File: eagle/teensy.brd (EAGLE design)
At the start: 63.5 x 49.2 mm, 3 parts, among them SW2 282834-2

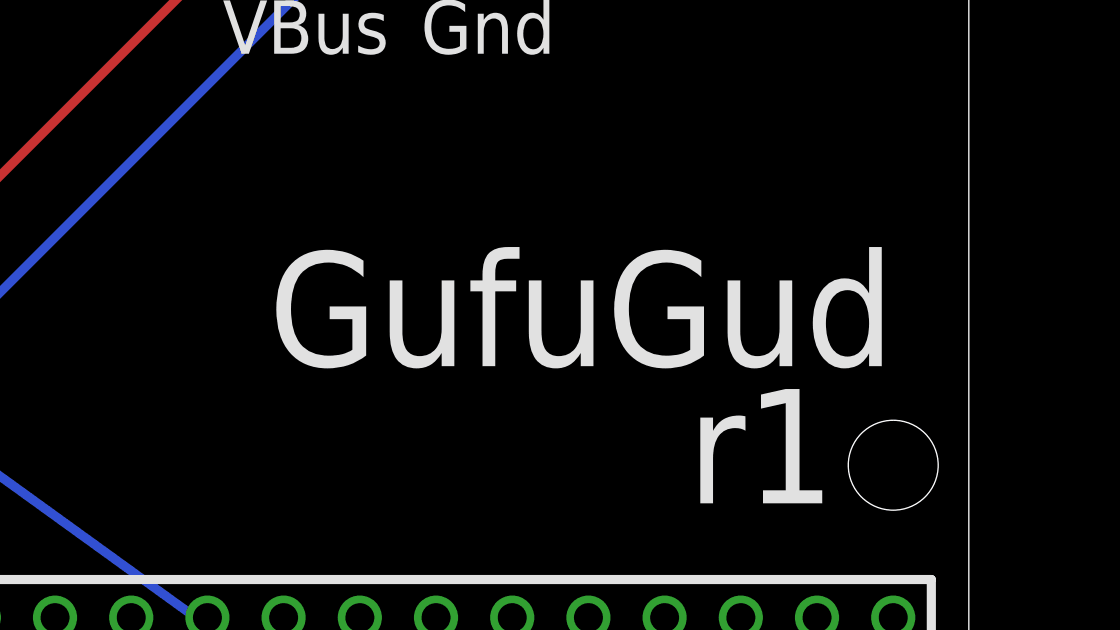
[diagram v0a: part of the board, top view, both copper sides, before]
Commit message: update and sync all schematics and images - fix labels and add consistent attribution
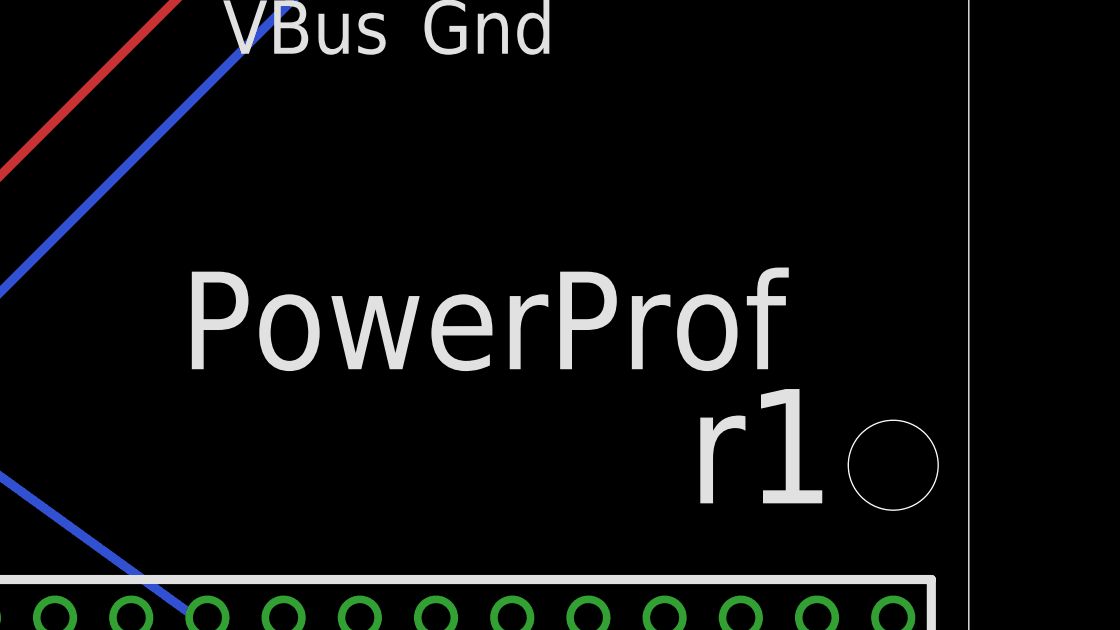
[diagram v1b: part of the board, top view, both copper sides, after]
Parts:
- SW2: value 282834-2 -> (none)
- renumbered U$1 to U1
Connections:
- net N$1 renamed VCC
- net N$2 renamed GND
- net N$3 renamed SCL
- net N$4 renamed SDA
- net N$5 renamed ALERT
- net N$8 renamed VBUS
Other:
- board text added: "MIT License - by ayan4m1"
- board text added: "PowerProf"
- board text added: "https://github.com/powerprof"
- board text removed: "GufuGud"
- board text removed: "by ayan4m1 and weeding_nerdy"

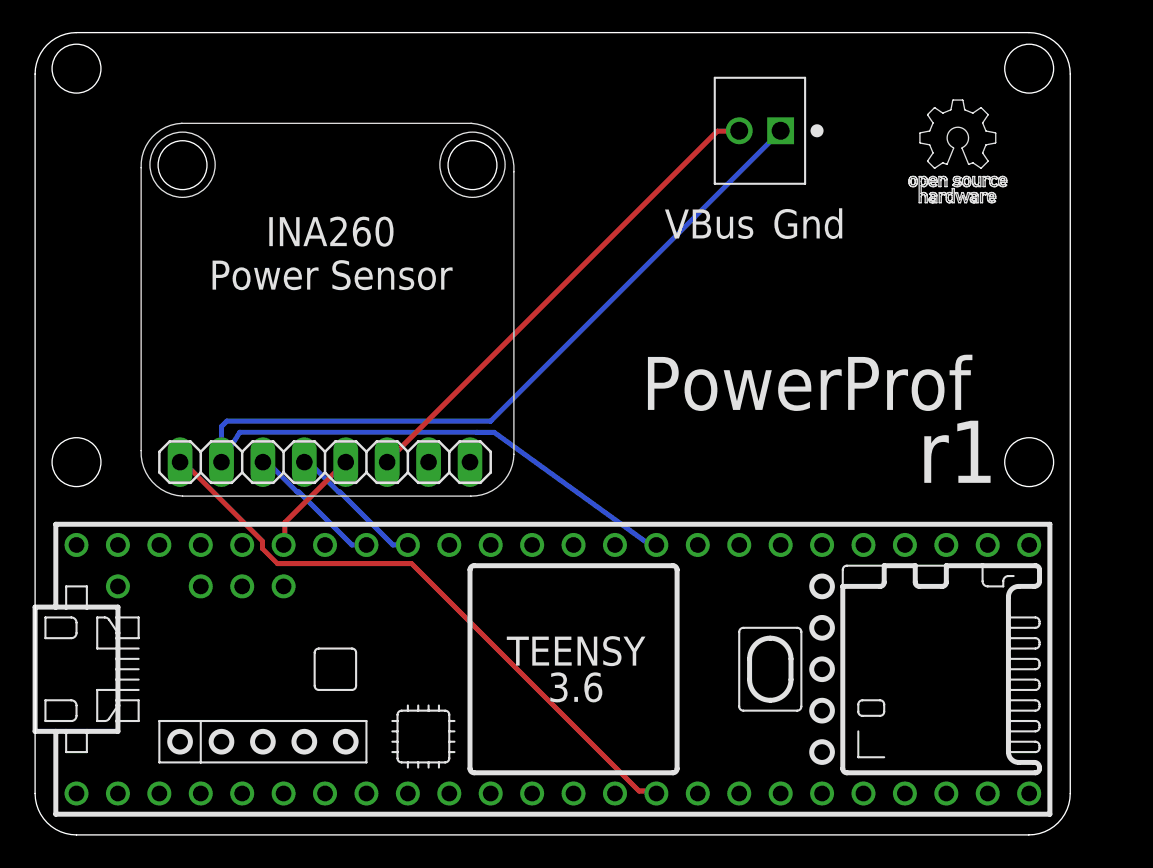
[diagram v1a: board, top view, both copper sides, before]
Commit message: update clearances to 8mil (thanks tech-tx!)
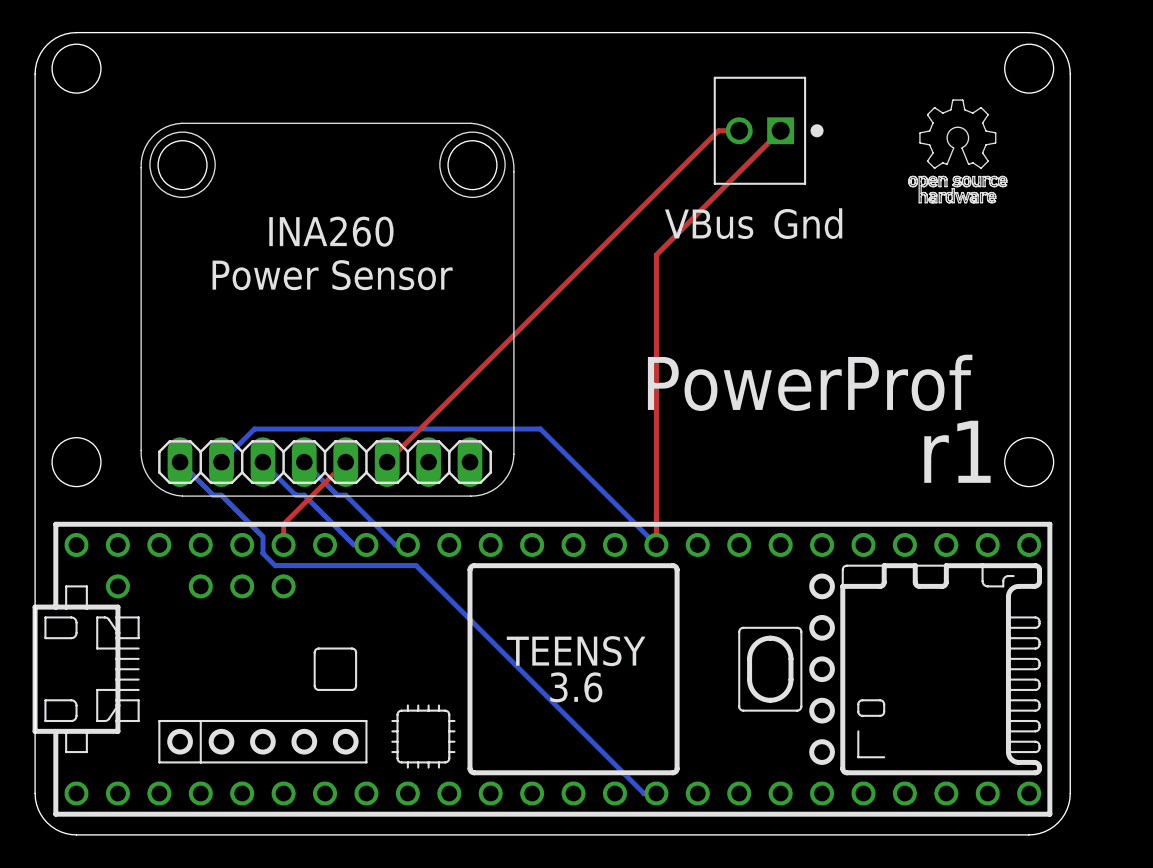
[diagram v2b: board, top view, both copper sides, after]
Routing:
- net GND: track 74.0 -> 59.0 mm
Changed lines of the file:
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@@
 <param name="mtCopper" value="0.035mm 0.035mm 0.035mm 0.035mm 0.035mm 0.035mm 0.035mm 0.035mm 0.035mm 0.035mm 0.035mm 0.035mm 0.035mm 0.035mm 0.035mm 0.035mm"/>
 <param name="mtIsolate" value="1.5mm 0.15mm 0.2mm 0.15mm 0.2mm 0.15mm 0.2mm 0.15mm 0.2mm 0.15mm 0.2mm 0.15mm 0.2mm 0.15mm 0.2mm"/>
-<param name="mdWireWire" value="6mil"/>
-<param name="mdWirePad" value="6mil"/>
-<param name="mdWireVia" value="6mil"/>
-<param name="mdPadPad" value="6mil"/>
-<param name="mdPadVia" value="6mil"/>
-<param name="mdViaVia" value="6mil"/>
-<param name="mdSmdPad" value="6mil"/>
-<param name="mdSmdVia" value="6mil"/>
-<param name="mdSmdSmd" value="6mil"/>
+<param name="mdWireWire" value="8mil"/>
+<param name="mdWirePad" value="8mil"/>
+<param name="mdWireVia" value="8mil"/>
+<param name="mdPadPad" value="8mil"/>
+<param name="mdPadVia" value="8mil"/>
+<param name="mdViaVia" value="8mil"/>
+<param name="mdSmdPad" value="8mil"/>
+<param name="mdSmdVia" value="8mil"/>
+<param name="mdSmdSmd" value="8mil"/>
 <param name="mdViaViaSameLayer" value="6mil"/>
 <param name="mnLayersViaInSmd" value="2"/>
@@
 <signal name="VCC">
 <contactref element="U1" pad="3V3"/>
-<wire x1="37.0332" y1="53.4924" x2="37.9476" y2="53.4924" width="0.3048" layer="1"/>
-<wire x1="23.0886" y1="67.437" x2="37.0332" y2="53.4924" width="0.3048" layer="1"/>
-<wire x1="14.859" y1="67.437" x2="23.0886" y2="67.437" width="0.3048" layer="1"/>
-<wire x1="13.9446" y1="68.3514" x2="14.859" y2="67.437" width="0.3048" layer="1"/>
-<wire x1="13.9446" y1="68.8086" x2="13.9446" y2="68.3514" width="0.3048" layer="1"/>
-<wire x1="8.9154" y1="73.8378" x2="13.9446" y2="68.8086" width="0.3048" layer="1"/>
-<wire x1="37.9476" y1="53.4924" x2="38.1" y2="53.34" width="0.3048" layer="1"/>
 <contactref element="JP1" pad="1"/>
-<wire x1="8.9154" y1="73.8378" x2="8.89" y2="73.66" width="0.3048" layer="1"/>
+<wire x1="37.338" y1="53.34" x2="38.1" y2="53.34" width="0.3048" layer="16"/>
+<wire x1="23.368" y1="67.31" x2="37.338" y2="53.34" width="0.3048" layer="16"/>
+<wire x1="14.732" y1="67.31" x2="23.368" y2="67.31" width="0.3048" layer="16"/>
+<wire x1="13.97" y1="68.072" x2="14.732" y2="67.31" width="0.3048" layer="16"/>
+<wire x1="13.97" y1="69.088" x2="13.97" y2="68.072" width="0.3048" layer="16"/>
+<wire x1="11.43" y1="71.628" x2="13.97" y2="69.088" width="0.3048" layer="16"/>
+<wire x1="10.922" y1="71.628" x2="11.43" y2="71.628" width="0.3048" layer="16"/>
+<wire x1="8.89" y1="73.66" x2="10.922" y2="71.628" width="0.3048" layer="16"/>
 </signal>
 <signal name="GND">
 <contactref element="SW2" pad="1"/>
 <contactref element="U1" pad="GND2"/>
-<wire x1="38.1762" y1="68.58" x2="38.1" y2="68.58" width="0.3048" layer="16"/>
-<wire x1="45.72" y1="93.98" x2="45.72" y2="93.9546" width="0.3048" layer="16"/>
-<wire x1="45.72" y1="93.9546" x2="27.94" y2="76.1746" width="0.3048" layer="16"/>
-<wire x1="27.94" y1="76.1746" x2="11.7602" y2="76.1746" width="0.3048" layer="16"/>
-<wire x1="11.43" y1="75.8444" x2="11.43" y2="73.66" width="0.3048" layer="16"/>
 <contactref element="JP1" pad="2"/>
-<wire x1="37.713109375" y1="68.58" x2="38.1" y2="68.58" width="0.3048" layer="16"/>
-<wire x1="37.713109375" y1="68.58" x2="28.153121875" y2="75.487215625" width="0.3048" layer="16"/>
-<wire x1="28.153121875" y1="75.487215625" x2="27.113471875" y2="75.487215625" width="0.3048" layer="16"/>
-<wire x1="27.113471875" y1="75.487215625" x2="27.1118875" y2="75.4888" width="0.3048" layer="16"/>
-<wire x1="12.5476" y1="75.4888" x2="11.43" y2="73.66" width="0.3048" layer="16"/>
-<wire x1="27.1118875" y1="75.4888" x2="12.5476" y2="75.4888" width="0.3048" layer="16"/>
-<wire x1="11.7602" y1="76.1746" x2="11.43" y2="75.8444" width="0.3048" layer="16"/>
+<wire x1="38.1" y1="86.36" x2="38.1" y2="68.58" width="0.3048" layer="1"/>
+<wire x1="45.72" y1="93.98" x2="38.1" y2="86.36" width="0.3048" layer="1"/>
+<wire x1="13.462" y1="75.692" x2="11.43" y2="73.66" width="0.3048" layer="16"/>
+<wire x1="30.988" y1="75.692" x2="13.462" y2="75.692" width="0.3048" layer="16"/>
+<wire x1="38.1" y1="68.58" x2="30.988" y2="75.692" width="0.3048" layer="16"/>
 </signal>
 <signal name="SCL">
 <contactref element="U1" pad="19/A5/SCL"/>
-<wire x1="20.32" y1="68.58" x2="19.431" y2="68.58" width="0.3048" layer="16"/>
 <contactref element="JP1" pad="3"/>
-<wire x1="14.1732" y1="73.6092" x2="13.97" y2="73.66" width="0.3048" layer="16"/>
-<wire x1="16.1798" y1="71.8312" x2="16.0681125" y2="71.8312" width="0.3048" layer="16"/>
-<wire x1="14.2393125" y1="73.66" x2="13.97" y2="73.66" width="0.3048" layer="16"/>
-<wire x1="16.0681125" y1="71.8312" x2="14.2393125" y2="73.66" width="0.3048" layer="16"/>
-<wire x1="19.431" y1="68.58" x2="16.1798" y2="71.8312" width="0.3048" layer="16"/>
+<wire x1="19.558" y1="68.58" x2="20.32" y2="68.58" width="0.3048" layer="16"/>
+<wire x1="16.51" y1="71.628" x2="19.558" y2="68.58" width="0.3048" layer="16"/>
+<wire x1="16.002" y1="71.628" x2="16.51" y2="71.628" width="0.3048" layer="16"/>
+<wire x1="13.97" y1="73.66" x2="16.002" y2="71.628" width="0.3048" layer="16"/>
 </signal>
 <signal name="SDA">
 <contactref element="U1" pad="18/A4/SDA"/>
-<wire x1="22.86" y1="68.58" x2="21.9456" y2="68.58" width="0.3048" layer="16"/>
 <contactref element="JP1" pad="4"/>
-<wire x1="16.6878" y1="73.6092" x2="16.51" y2="73.66" width="0.3048" layer="16"/>
-<wire x1="18.6944" y1="71.8312" x2="18.6081125" y2="71.8312" width="0.3048" layer="16"/>
-<wire x1="16.7793125" y1="73.66" x2="16.51" y2="73.66" width="0.3048" layer="16"/>
-<wire x1="18.6081125" y1="71.8312" x2="16.7793125" y2="73.66" width="0.3048" layer="16"/>
-<wire x1="21.9456" y1="68.58" x2="18.6944" y2="71.8312" width="0.3048" layer="16"/>
+<wire x1="22.098" y1="68.58" x2="22.86" y2="68.58" width="0.3048" layer="16"/>
+<wire x1="19.05" y1="71.628" x2="22.098" y2="68.58" width="0.3048" layer="16"/>
+<wire x1="18.542" y1="71.628" x2="19.05" y2="71.628" width="0.3048" layer="16"/>
+<wire x1="16.51" y1="73.66" x2="18.542" y2="71.628" width="0.3048" layer="16"/>
 </signal>
 <signal name="VBUS">
 <contactref element="SW2" pad="2"/>
-<wire x1="41.8338" y1="93.9546" x2="21.717" y2="73.8378" width="0.3048" layer="1"/>
-<wire x1="42.9768" y1="93.9546" x2="41.8338" y2="93.9546" width="0.3048" layer="1"/>
-<wire x1="42.9768" y1="93.9546" x2="43.18" y2="93.98" width="0.3048" layer="1"/>
 <contactref element="JP1" pad="6"/>
-<wire x1="21.717" y1="73.8378" x2="21.59" y2="73.66" width="0.3048" layer="1"/>
+<wire x1="41.91" y1="93.98" x2="21.59" y2="73.66" width="0.3048" layer="1"/>
+<wire x1="43.18" y1="93.98" x2="41.91" y2="93.98" width="0.3048" layer="1"/>
 </signal>
 <signal name="ALERT">
 <contactref element="JP1" pad="5"/>
 <contactref element="U1" pad="21/A7"/>
-<wire x1="15.3162" y1="69.9516" x2="15.3162" y2="68.58" width="0.3048" layer="1"/>
-<wire x1="18.9738" y1="73.6092" x2="15.3162" y2="69.9516" width="0.3048" layer="1"/>
-<wire x1="15.3162" y1="68.58" x2="15.24" y2="68.58" width="0.3048" layer="1"/>
-<wire x1="18.9738" y1="73.6092" x2="19.05" y2="73.66" width="0.3048" layer="1"/>
+<wire x1="15.24" y1="69.85" x2="15.24" y2="68.58" width="0.3048" layer="1"/>
+<wire x1="19.05" y1="73.66" x2="15.24" y2="69.85" width="0.3048" layer="1"/>
 </signal>
 </signals>

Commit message: sync boards to use same net classes, update images with new traces
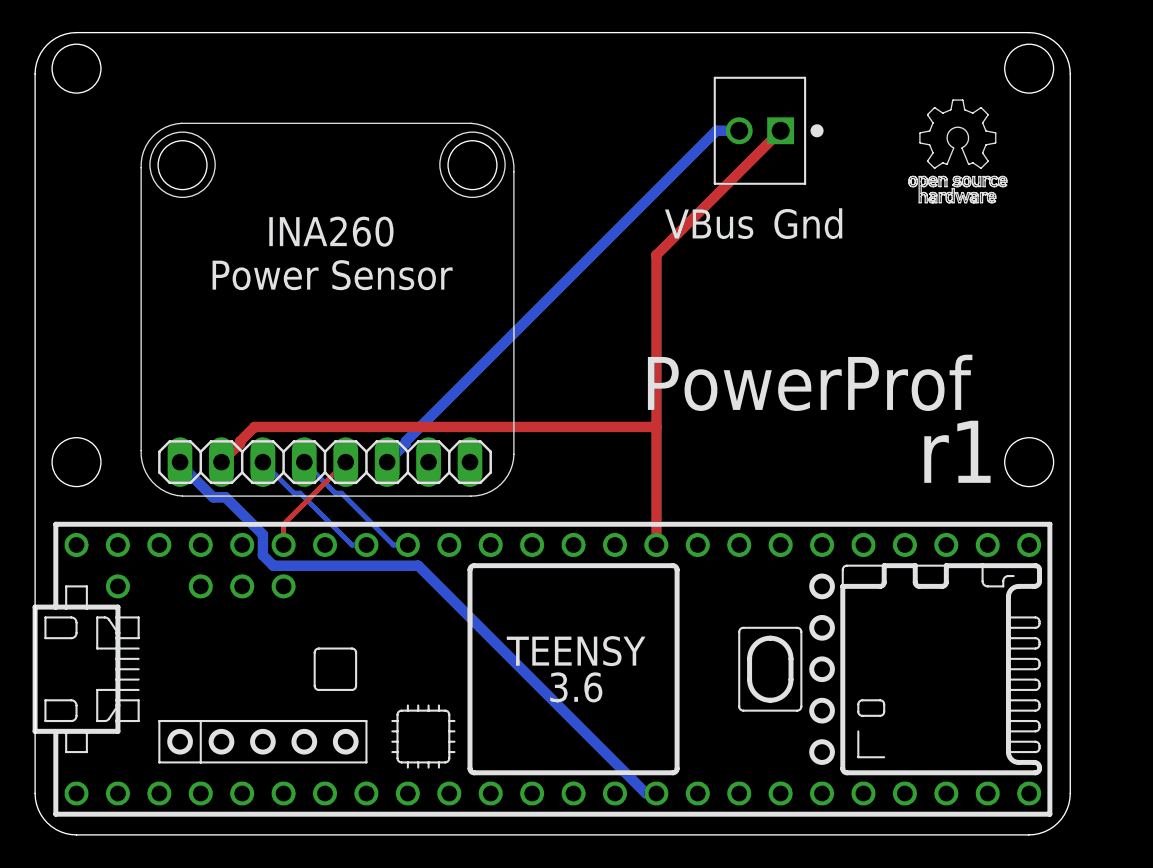
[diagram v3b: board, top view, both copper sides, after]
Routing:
- net GND: track 59.0 -> 56.2 mm
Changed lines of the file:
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@@
 </variantdefs>
 <classes>
-<class number="0" name="default" width="0" drill="0">
+<class number="0" name="default" width="0.1524" drill="0">
 </class>
-<class number="1" name="signal" width="0" drill="0">
+<class number="1" name="signal" width="0.2032" drill="0">
 </class>
-<class number="2" name="current" width="0" drill="0">
+<class number="2" name="current" width="0.635" drill="0">
 </class>
 </classes>
@@
 <param name="RoutingGrid" value="50mil"/>
 <param name="AutoGrid" value="1"/>
-<param name="Efforts" value="0"/>
+<param name="Efforts" value="2"/>
 <param name="TopRouterVariant" value="1"/>
 <param name="tpViaShape" value="round"/>
@@
 </elements>
 <signals>
-<signal name="VCC">
+<signal name="VCC" class="2">
 <contactref element="U1" pad="3V3"/>
 <contactref element="JP1" pad="1"/>
-<wire x1="37.338" y1="53.34" x2="38.1" y2="53.34" width="0.3048" layer="16"/>
-<wire x1="23.368" y1="67.31" x2="37.338" y2="53.34" width="0.3048" layer="16"/>
-<wire x1="14.732" y1="67.31" x2="23.368" y2="67.31" width="0.3048" layer="16"/>
-<wire x1="13.97" y1="68.072" x2="14.732" y2="67.31" width="0.3048" layer="16"/>
-<wire x1="13.97" y1="69.088" x2="13.97" y2="68.072" width="0.3048" layer="16"/>
-<wire x1="11.43" y1="71.628" x2="13.97" y2="69.088" width="0.3048" layer="16"/>
-<wire x1="10.922" y1="71.628" x2="11.43" y2="71.628" width="0.3048" layer="16"/>
-<wire x1="8.89" y1="73.66" x2="10.922" y2="71.628" width="0.3048" layer="16"/>
-</signal>
-<signal name="GND">
+<wire x1="37.465" y1="53.34" x2="38.1" y2="53.34" width="0.635" layer="16"/>
+<wire x1="23.495" y1="67.31" x2="37.465" y2="53.34" width="0.635" layer="16"/>
+<wire x1="14.605" y1="67.31" x2="23.495" y2="67.31" width="0.635" layer="16"/>
+<wire x1="13.97" y1="67.945" x2="14.605" y2="67.31" width="0.635" layer="16"/>
+<wire x1="13.97" y1="69.215" x2="13.97" y2="67.945" width="0.635" layer="16"/>
+<wire x1="11.684" y1="71.501" x2="13.97" y2="69.215" width="0.635" layer="16"/>
+<wire x1="10.922" y1="71.501" x2="11.684" y2="71.501" width="0.635" layer="16"/>
+<wire x1="8.89" y1="73.533" x2="10.922" y2="71.501" width="0.635" layer="16"/>
+<wire x1="8.89" y1="73.66" x2="8.89" y2="73.533" width="0.635" layer="16"/>
+</signal>
+<signal name="GND" class="2">
 <contactref element="SW2" pad="1"/>
 <contactref element="U1" pad="GND2"/>
 <contactref element="JP1" pad="2"/>
-<wire x1="38.1" y1="86.36" x2="38.1" y2="68.58" width="0.3048" layer="1"/>
-<wire x1="45.72" y1="93.98" x2="38.1" y2="86.36" width="0.3048" layer="1"/>
-<wire x1="13.462" y1="75.692" x2="11.43" y2="73.66" width="0.3048" layer="16"/>
-<wire x1="30.988" y1="75.692" x2="13.462" y2="75.692" width="0.3048" layer="16"/>
-<wire x1="38.1" y1="68.58" x2="30.988" y2="75.692" width="0.3048" layer="16"/>
-</signal>
-<signal name="SCL">
+<wire x1="38.1" y1="86.36" x2="38.1" y2="75.819" width="0.635" layer="1"/>
+<wire x1="38.1" y1="75.819" x2="38.1" y2="68.58" width="0.635" layer="1"/>
+<wire x1="45.72" y1="93.98" x2="38.1" y2="86.36" width="0.635" layer="1"/>
+<wire x1="12.573" y1="74.803" x2="11.43" y2="73.66" width="0.635" layer="1"/>
+<wire x1="12.573" y1="74.93" x2="12.573" y2="74.803" width="0.635" layer="1"/>
+<wire x1="13.462" y1="75.819" x2="12.573" y2="74.93" width="0.635" layer="1"/>
+<wire x1="38.1" y1="75.819" x2="13.462" y2="75.819" width="0.635" layer="1"/>
+</signal>
+<signal name="SCL" class="1">
 <contactref element="U1" pad="19/A5/SCL"/>
 <contactref element="JP1" pad="3"/>
-<wire x1="19.558" y1="68.58" x2="20.32" y2="68.58" width="0.3048" layer="16"/>
-<wire x1="16.51" y1="71.628" x2="19.558" y2="68.58" width="0.3048" layer="16"/>
-<wire x1="16.002" y1="71.628" x2="16.51" y2="71.628" width="0.3048" layer="16"/>
-<wire x1="13.97" y1="73.66" x2="16.002" y2="71.628" width="0.3048" layer="16"/>
-</signal>
-<signal name="SDA">
+<wire x1="19.431" y1="68.58" x2="20.32" y2="68.58" width="0.3048" layer="16"/>
+<wire x1="16.256" y1="71.755" x2="19.431" y2="68.58" width="0.3048" layer="16"/>
+<wire x1="15.875" y1="71.755" x2="16.256" y2="71.755" width="0.3048" layer="16"/>
+<wire x1="13.97" y1="73.66" x2="15.875" y2="71.755" width="0.3048" layer="16"/>
+</signal>
+<signal name="SDA" class="1">
 <contactref element="U1" pad="18/A4/SDA"/>
 <contactref element="JP1" pad="4"/>
-<wire x1="22.098" y1="68.58" x2="22.86" y2="68.58" width="0.3048" layer="16"/>
-<wire x1="19.05" y1="71.628" x2="22.098" y2="68.58" width="0.3048" layer="16"/>
-<wire x1="18.542" y1="71.628" x2="19.05" y2="71.628" width="0.3048" layer="16"/>
-<wire x1="16.51" y1="73.66" x2="18.542" y2="71.628" width="0.3048" layer="16"/>
-</signal>
-<signal name="VBUS">
+<wire x1="21.971" y1="68.58" x2="22.86" y2="68.58" width="0.3048" layer="16"/>
+<wire x1="18.796" y1="71.755" x2="21.971" y2="68.58" width="0.3048" layer="16"/>
+<wire x1="18.415" y1="71.755" x2="18.796" y2="71.755" width="0.3048" layer="16"/>
+<wire x1="16.51" y1="73.66" x2="18.415" y2="71.755" width="0.3048" layer="16"/>
+</signal>
+<signal name="VBUS" class="2">
 <contactref element="SW2" pad="2"/>
 <contactref element="JP1" pad="6"/>
-<wire x1="41.91" y1="93.98" x2="21.59" y2="73.66" width="0.3048" layer="1"/>
-<wire x1="43.18" y1="93.98" x2="41.91" y2="93.98" width="0.3048" layer="1"/>
-</signal>
-<signal name="ALERT">
+<wire x1="22.733" y1="74.803" x2="21.59" y2="73.66" width="0.635" layer="16"/>
+<wire x1="22.733" y1="74.93" x2="22.733" y2="74.803" width="0.635" layer="16"/>
+<wire x1="41.783" y1="93.98" x2="22.733" y2="74.93" width="0.635" layer="16"/>
+<wire x1="43.18" y1="93.98" x2="41.783" y2="93.98" width="0.635" layer="16"/>
+</signal>
+<signal name="ALERT" class="1">
 <contactref element="JP1" pad="5"/>
 <contactref element="U1" pad="21/A7"/>
